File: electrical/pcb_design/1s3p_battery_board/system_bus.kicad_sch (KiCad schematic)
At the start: 2 parts, among them J2 Molex_504050-1291, J3 Molex_504050-1291

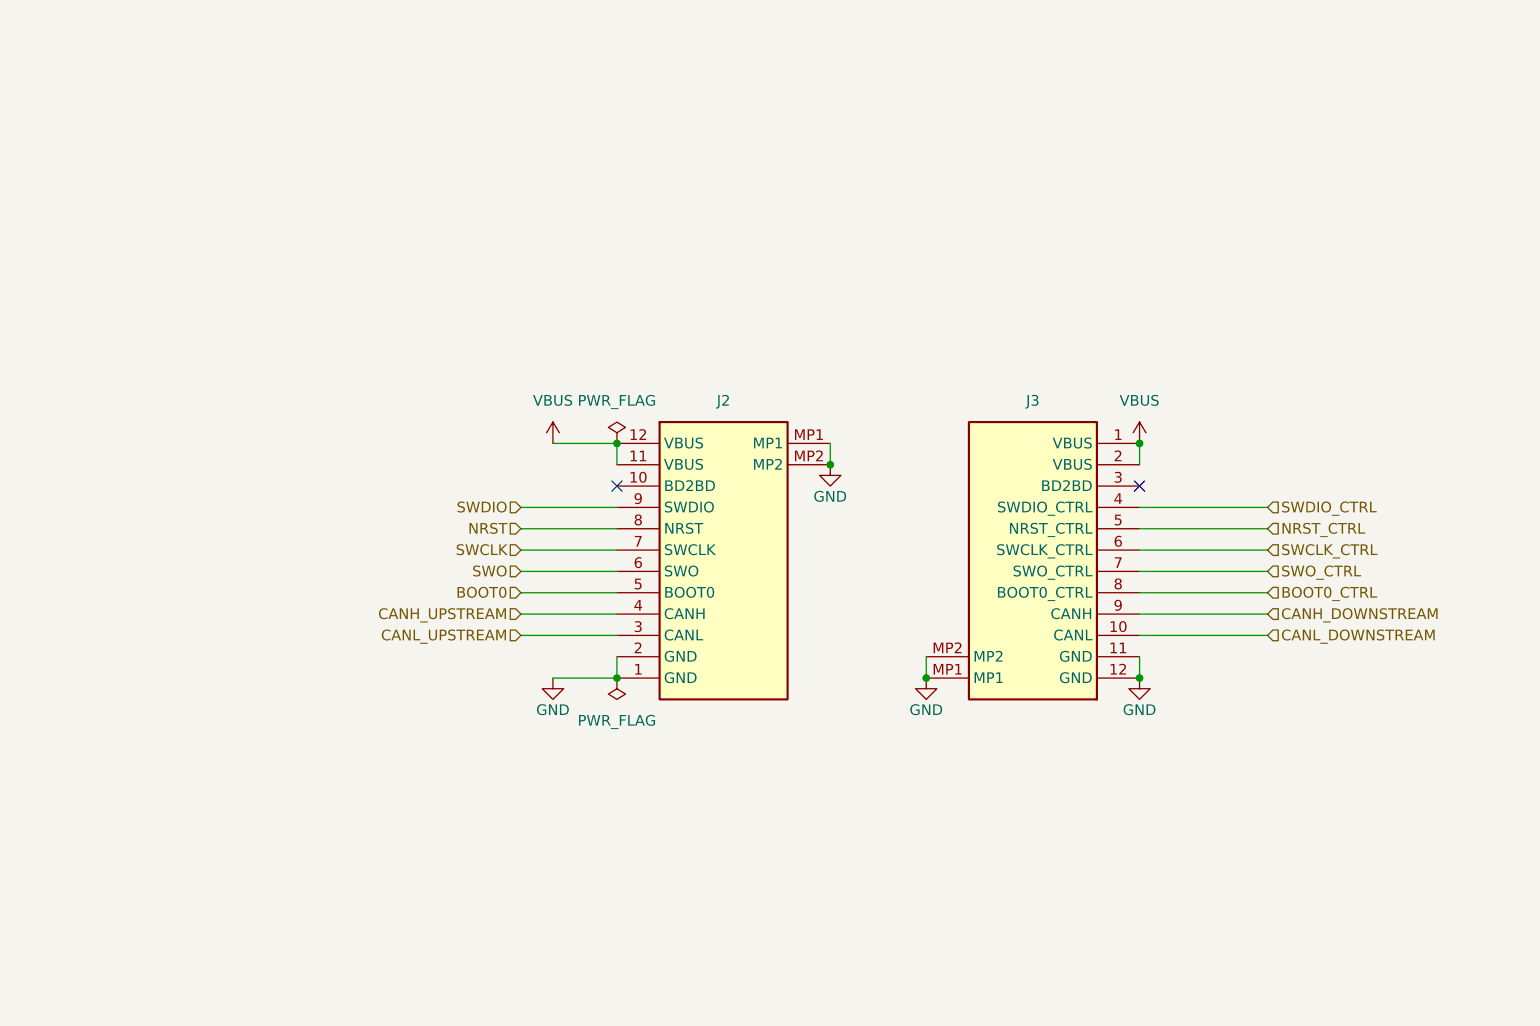
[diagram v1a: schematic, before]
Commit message: Restructure battery board with new system bus, power monitoring chip, and battery charging IC.
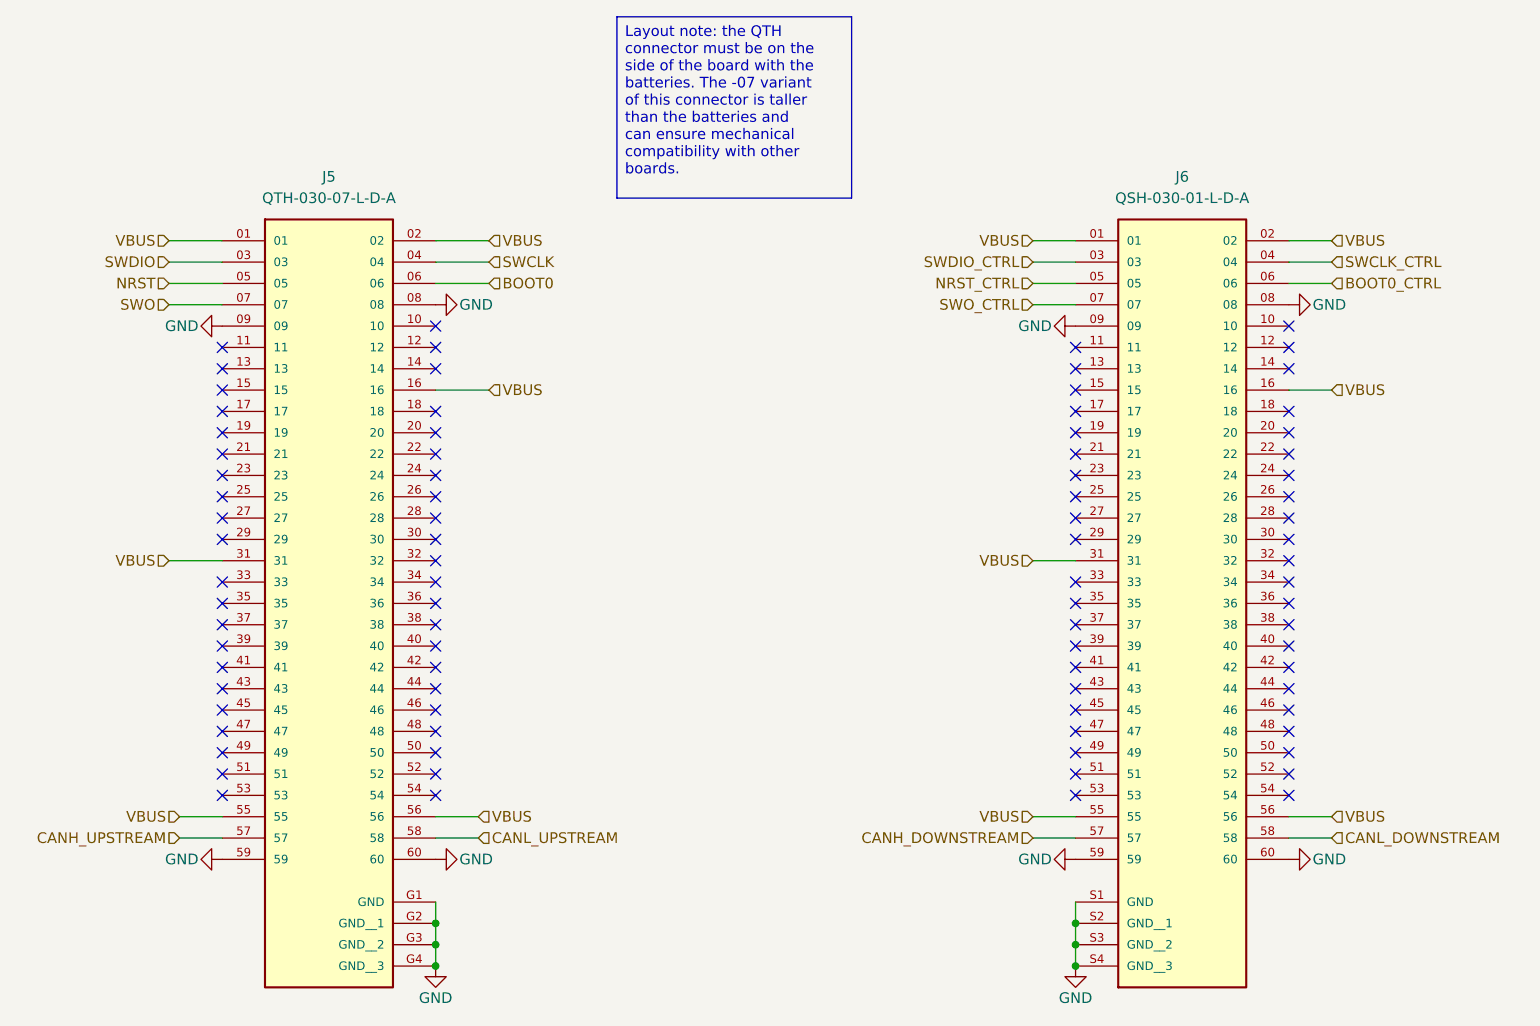
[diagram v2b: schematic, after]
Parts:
- removed J2: Molex_504050-1291, footprints:Bus Connector (Target), symbol TVSC:Bus Connector (Target)
- removed J3: Molex_504050-1291, footprints:Bus Connector (Control), symbol TVSC:Bus Connector (Control)
- added J5: QTH-030-07-L-D-A, footprints:SAMTEC_QTH-030-07-L-D-A, symbol TVSC:QTH-030-07-L-D-A
- added J6: QSH-030-01-L-D-A, footprints:SAMTEC_QSH-030-01-L-D-A, symbol TVSC:QSH-030-01-L-D-A
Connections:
- net BOOT0: now also J5.06
- net BOOT0_CTRL: now also J6.06
- net CANH_DOWNSTREAM: now also J6.57
- net CANH_UPSTREAM: now also J5.57
- net CANL_DOWNSTREAM: now also J6.58
- net CANL_UPSTREAM: now also J5.58
- net GND: now also J5.08, J5.09, J5.59, J5.60, J5.G1 (GND), J5.G2 (GND__1), J5.G3 (GND__2), J5.G4 (GND__3), J6.08, J6.09, J6.59, J6.60, J6.S1 (GND), J6.S2 (GND__1), J6.S3 (GND__2), J6.S4 (GND__3)
- net NRST: now also J5.05
- net NRST_CTRL: now also J6.05
- net SWCLK: now also J5.04
- net SWCLK_CTRL: now also J6.04
- net SWDIO: now also J5.03
- net SWDIO_CTRL: now also J6.03
- net SWO: now also J5.07
- net SWO_CTRL: now also J6.07
- net VBUS: now also J5.01, J5.02, J5.16, J5.31, J5.55, J5.56, J6.01, J6.02, J6.16, J6.31, J6.55, J6.56
- no-connect marks 2 -> 86

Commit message: Fix schematic page titles, paper size, etc. of 1s3p battery board.
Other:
- company: (none) -> TVSC
- title: (none) -> 1s3p Battery Board
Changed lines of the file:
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@@
 	(generator_version "9.0")
 	(paper "USLetter")
+	(title_block
+		(title "1s3p Battery Board")
+		(date "2026-07-11")
+		(rev "${PCB_VERSION}")
+		(company "TVSC")
+	)
 	(text_box "Layout note: the QTH connector must be on the side of the board with the batteries. The -07 variant of this connector is taller than the batteries and can ensure mechanical compatibility with other boards."
 		(exclude_from_sim no)

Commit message: Checkpoint progress on battery board. Preparing to break out reusable functional modules.
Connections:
- net CANH_DOWNSTREAM: now also J6.56; no longer J6.57
- net CANH_UPSTREAM: now also J5.56; no longer J5.57
- net VBUS: now also J5.54, J6.54; no longer J5.55, J5.56, J6.55, J6.56
- net VSOLAR_1: now reaches J6.18
- net VSOLAR_1: now also J5.18
- net VSOLAR_2: now reaches J6.20
- net VSOLAR_2: now also J5.20
- net VSOLAR_3: now reaches J6.22
- net VSOLAR_3: now also J5.22
- net VSOLAR_4: now reaches J6.24
- net VSOLAR_4: now also J5.24
- net VSOLAR_5: now reaches J6.26
- net VSOLAR_5: now also J5.26
- net VSOLAR_6: now reaches J6.28
- net VSOLAR_6: now also J5.28
- no-connect marks 86 -> 70
